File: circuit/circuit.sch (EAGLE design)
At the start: 76 parts

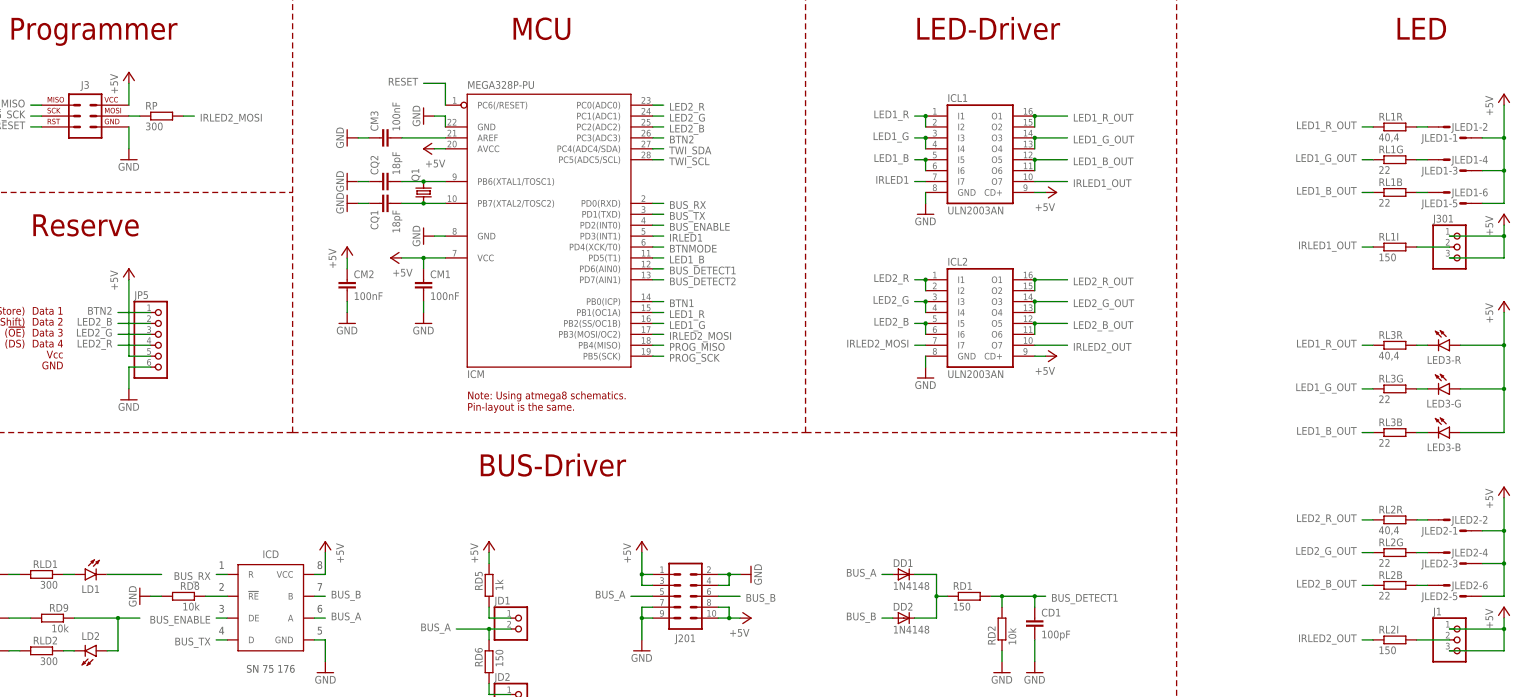
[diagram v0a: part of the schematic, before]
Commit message: updated circuit   + added layout (not done yet)
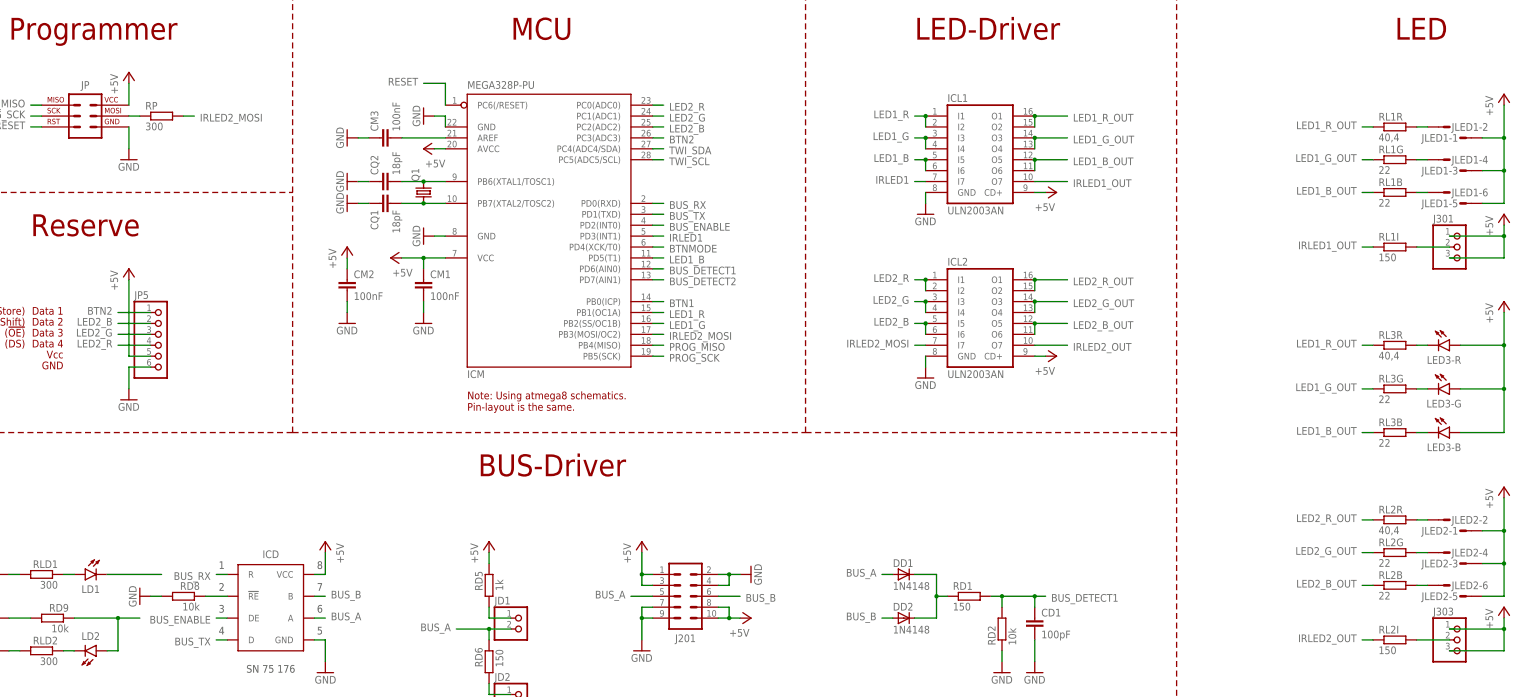
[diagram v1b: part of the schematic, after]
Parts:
- renumbered J1 to J303, J3 to JP
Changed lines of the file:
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@@
 <part name="GND15" library="supply1" deviceset="GND" device=""/>
 <part name="P+6" library="supply1" deviceset="+5V" device=""/>
-<part name="J3" library="robo_ag" deviceset="STECKER_ISP_6" device=""/>
+<part name="JP" library="robo_ag" deviceset="STECKER_ISP_6" device=""/>
 <part name="P+7" library="supply1" deviceset="+5V" device=""/>
 <part name="GND16" library="supply1" deviceset="GND" device=""/>
@@
 <part name="RL2B" library="rcl" deviceset="R-EU_" device="0207/10" value="22"/>
 <part name="P+15" library="supply1" deviceset="+5V" device=""/>
-<part name="J1" library="pinhead" deviceset="PINHD-1X3" device=""/>
+<part name="J303" library="pinhead" deviceset="PINHD-1X3" device=""/>
 <part name="P+17" library="supply1" deviceset="+5V" device=""/>
 <part name="RL3R" library="rcl" deviceset="R-EU_" device="0207/10" value="40,4"/>
@@
 <instance part="GND15" gate="1" x="353.06" y="208.28"/>
 <instance part="P+6" gate="1" x="353.06" y="243.84"/>
-<instance part="J3" gate="ISP" x="33.02" y="172.72"/>
+<instance part="JP" gate="ISP" x="33.02" y="172.72"/>
 <instance part="P+7" gate="1" x="111.76" y="165.1" rot="R90"/>
 <instance part="GND16" gate="1" x="93.98" y="167.64" rot="R270"/>
@@
 <instance part="RL2B" gate="G$1" x="337.82" y="63.5"/>
 <instance part="P+15" gate="1" x="363.22" y="86.36"/>
-<instance part="J1" gate="A" x="353.06" y="50.8"/>
+<instance part="J303" gate="A" x="353.06" y="50.8"/>
 <instance part="P+17" gate="1" x="363.22" y="58.42"/>
 <instance part="RL3R" gate="G$1" x="337.82" y="119.38"/>
@@
 </segment>
 <segment>
-<pinref part="J1" gate="A" pin="3"/>
+<pinref part="J303" gate="A" pin="3"/>
 <wire x1="350.52" y1="48.26" x2="363.22" y2="48.26" width="0.1524" layer="91"/>
 <wire x1="363.22" y1="53.34" x2="363.22" y2="48.26" width="0.1524" layer="91"/>
-<pinref part="J1" gate="A" pin="1"/>
+<pinref part="J303" gate="A" pin="1"/>
 <wire x1="350.52" y1="53.34" x2="363.22" y2="53.34" width="0.1524" layer="91"/>
 <pinref part="P+17" gate="1" pin="+5V"/>
@@
 </segment>
 <segment>
-<pinref part="J3" gate="ISP" pin="2_VCC"/>
+<pinref part="JP" gate="ISP" pin="2_VCC"/>
 <pinref part="P+20" gate="1" pin="+5V"/>
 <wire x1="43.18" y1="175.26" x2="43.18" y2="180.34" width="0.1524" layer="91"/>
@@
 </segment>
 <segment>
-<pinref part="J3" gate="ISP" pin="6_GND"/>
+<pinref part="JP" gate="ISP" pin="6_GND"/>
 <pinref part="GND27" gate="1" pin="GND"/>
 <wire x1="43.18" y1="170.18" x2="43.18" y2="165.1" width="0.1524" layer="91"/>
@@
 </segment>
 <segment>
-<pinref part="J3" gate="ISP" pin="5_RST"/>
+<pinref part="JP" gate="ISP" pin="5_RST"/>
 <wire x1="22.86" y1="170.18" x2="20.32" y2="170.18" width="0.1524" layer="91"/>
 <label x="19.05" y="171.45" size="1.778" layer="91" rot="R180"/>
@@
 </segment>
 <segment>
-<pinref part="J3" gate="ISP" pin="1_MISO"/>
+<pinref part="JP" gate="ISP" pin="1_MISO"/>
 <wire x1="22.86" y1="175.26" x2="20.32" y2="175.26" width="0.1524" layer="91"/>
 <label x="19.05" y="176.53" size="1.778" layer="91" rot="R180"/>
@@
 </segment>
 <segment>
-<pinref part="J3" gate="ISP" pin="3_SCK"/>
+<pinref part="JP" gate="ISP" pin="3_SCK"/>
 <wire x1="22.86" y1="172.72" x2="20.32" y2="172.72" width="0.1524" layer="91"/>
 <label x="19.05" y="173.99" size="1.778" layer="91" rot="R180"/>
@@
 <net name="N$22" class="0">
 <segment>
-<pinref part="J1" gate="A" pin="2"/>
+<pinref part="J303" gate="A" pin="2"/>
 <wire x1="350.52" y1="50.8" x2="342.9" y2="50.8" width="0.1524" layer="91"/>
 <pinref part="RL2I" gate="G$1" pin="2"/>
@@
 <net name="PROG_MOSI_1" class="0">
 <segment>
-<pinref part="J3" gate="ISP" pin="4_MOSI"/>
+<pinref part="JP" gate="ISP" pin="4_MOSI"/>
 <wire x1="43.18" y1="172.72" x2="45.72" y2="172.72" width="0.1524" layer="91"/>
 <pinref part="RP" gate="G$1" pin="1"/>

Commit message: updated circuit   + layout is done   + updated export files
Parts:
- removed JP5: (no value), pinhead:PINHD-1X6/90
- added JP6: (no value), pinhead:PINHD-1X6/90
- added JT: (no value), pinhead:PINHD-1X4
- RD2: value 10k -> 100k
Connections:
- net +5V: now also JP6.5, LD1.A; no longer JP5.5
- net BTN2: now also JP6.1; no longer JP5.1
- net BUS_ENABLE: now also RLD2.1; no longer LD2.A
- net BUS_RX: now also RLD1.2; no longer LD1.C
- net GND: now also JP6.6, LD2.C; no longer JP5.6, RLD1.2, RLD2.2
- net LED2_B: now also JP6.2; no longer JP5.2
- net LED2_G: now also JP6.3; no longer JP5.3
- net LED2_R: now also JP6.4; no longer JP5.4
- net N$34: now also LD1.C, RLD1.1; no longer LD2.C, RLD2.1
- net N$37: now also LD2.A, RLD2.2; no longer LD1.A, RLD1.1
- net TWI_SCL: now also JT.1, JT.4
- net TWI_SDA: now also JT.2, JT.3
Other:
- note added: "Note: SN75176 & ADM485 share the same layout."
- note added: "Note: Value of RD3 and RD4 depend on ICD! SN75176: RD3= ; RD4= ADM485: RD3= ; RD4="
- moved on the sheet: LD1, LD2, RD9, RLD1, RLD2

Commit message: finished layout and exported data
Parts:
- added JD4: (no value), pinhead:PINHD-1X2
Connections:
- net BUS_DETECT1: now also JD4.2
- net LED2_R: now also JD4.1
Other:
- note added: "Note: Possible extended Bus-Detection through ADC-Pin 0. E.g. Idle-Detection. Only if in single-light-mode (not 2 lights). ==> Therefore using a jumper"
- moved on the sheet: CD1, DD1, DD2, RD1, RD2
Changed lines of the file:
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@@
 <part name="P+29" library="supply1" deviceset="+5V" device=""/>
 <part name="JT" library="pinhead" deviceset="PINHD-1X4" device=""/>
+<part name="JD4" library="pinhead" deviceset="PINHD-1X2" device=""/>
 </parts>
 <sheets>
@@
 SN75176: RD3=  ;  RD4=
 ADM485: RD3=  ;  RD4=</text>
+<text x="231.14" y="78.74" size="1.778" layer="94">Note: Possible extended Bus-Detection
+through ADC-Pin 0. E.g. Idle-Detection.
+Only if in single-light-mode (not 2 lights).
+==&gt; Therefore using a jumper</text>
 </plain>
 <instances>
@@
 <instance part="CQ2" gate="G$1" x="101.6" y="157.48" rot="R90"/>
 <instance part="ICL1" gate="A" x="241.3" y="165.1"/>
-<instance part="DD1" gate="G$1" x="223.52" y="66.04" smashed="yes">
-<attribute name="NAME" x="220.98" y="67.7926" size="1.778" layer="95"/>
-<attribute name="VALUE" x="220.98" y="62.4586" size="1.778" layer="96"/>
+<instance part="DD1" gate="G$1" x="223.52" y="60.96" smashed="yes">
+<attribute name="NAME" x="220.98" y="62.7126" size="1.778" layer="95"/>
+<attribute name="VALUE" x="220.98" y="57.3786" size="1.778" layer="96"/>
 </instance>
-<instance part="DD2" gate="G$1" x="223.52" y="55.88" smashed="yes">
-<attribute name="NAME" x="220.98" y="57.6326" size="1.778" layer="95"/>
-<attribute name="VALUE" x="220.98" y="52.2986" size="1.778" layer="96"/>
+<instance part="DD2" gate="G$1" x="223.52" y="50.8" smashed="yes">
+<attribute name="NAME" x="220.98" y="52.5526" size="1.778" layer="95"/>
+<attribute name="VALUE" x="220.98" y="47.2186" size="1.778" layer="96"/>
 </instance>
 <instance part="B1" gate="1" x="170.18" y="218.44"/>
@@
 <instance part="LD1" gate="LED" x="20.32" y="66.04" rot="MR0"/>
 <instance part="RLD1" gate="G$1" x="20.32" y="53.34" rot="MR270"/>
-<instance part="RD1" gate="G$1" x="238.76" y="60.96"/>
-<instance part="CD1" gate="G$1" x="254" y="55.88"/>
-<instance part="GND39" gate="1" x="246.38" y="43.18"/>
-<instance part="RD2" gate="G$1" x="246.38" y="53.34" rot="R90"/>
-<instance part="GND40" gate="1" x="254" y="43.18"/>
+<instance part="RD1" gate="G$1" x="238.76" y="55.88"/>
+<instance part="CD1" gate="G$1" x="254" y="50.8"/>
+<instance part="GND39" gate="1" x="246.38" y="38.1"/>
+<instance part="RD2" gate="G$1" x="246.38" y="48.26" rot="R90"/>
+<instance part="GND40" gate="1" x="254" y="38.1"/>
 <instance part="RD3" gate="G$1" x="238.76" y="27.94"/>
 <instance part="CD2" gate="G$1" x="254" y="22.86"/>
@@
 <instance part="P+29" gate="1" x="20.32" y="73.66" rot="MR0"/>
 <instance part="JT" gate="A" x="53.34" y="121.92" rot="R180"/>
+<instance part="JD4" gate="G$1" x="248.92" y="68.58" rot="R270"/>
 </instances>
 <busses>
@@
 <pinref part="GND39" gate="1" pin="GND"/>
 <pinref part="RD2" gate="G$1" pin="1"/>
-<wire x1="246.38" y1="48.26" x2="246.38" y2="45.72" width="0.1524" layer="91"/>
+<wire x1="246.38" y1="43.18" x2="246.38" y2="40.64" width="0.1524" layer="91"/>
 </segment>
 <segment>
 <pinref part="CD1" gate="G$1" pin="2"/>
 <pinref part="GND40" gate="1" pin="GND"/>
-<wire x1="254" y1="50.8" x2="254" y2="45.72" width="0.1524" layer="91"/>
+<wire x1="254" y1="45.72" x2="254" y2="40.64" width="0.1524" layer="91"/>
 </segment>
 <segment>
@@
 <pinref part="RD1" gate="G$1" pin="2"/>
 <pinref part="CD1" gate="G$1" pin="1"/>
-<wire x1="243.84" y1="60.96" x2="246.38" y2="60.96" width="0.1524" layer="91"/>
+<wire x1="243.84" y1="55.88" x2="246.38" y2="55.88" width="0.1524" layer="91"/>
 <pinref part="RD2" gate="G$1" pin="2"/>
-<wire x1="246.38" y1="58.42" x2="246.38" y2="60.96" width="0.1524" layer="91"/>
-<junction x="246.38" y="60.96"/>
-<wire x1="254" y1="58.42" x2="254" y2="60.96" width="0.1524" layer="91"/>
-<wire x1="254" y1="60.96" x2="246.38" y2="60.96" width="0.1524" layer="91"/>
-<wire x1="254" y1="60.96" x2="256.54" y2="60.96" width="0.1524" layer="91"/>
-<junction x="254" y="60.96"/>
-<label x="257.81" y="59.69" size="1.778" layer="91"/>
+<wire x1="246.38" y1="53.34" x2="246.38" y2="55.88" width="0.1524" layer="91"/>
+<junction x="246.38" y="55.88"/>
+<wire x1="254" y1="53.34" x2="254" y2="55.88" width="0.1524" layer="91"/>
+<wire x1="254" y1="55.88" x2="246.38" y2="55.88" width="0.1524" layer="91"/>
+<wire x1="254" y1="55.88" x2="256.54" y2="55.88" width="0.1524" layer="91"/>
+<junction x="254" y="55.88"/>
+<label x="257.81" y="54.61" size="1.778" layer="91"/>
+</segment>
+<segment>
+<pinref part="JD4" gate="G$1" pin="2"/>
+<wire x1="248.92" y1="71.12" x2="241.3" y2="71.12" width="0.1524" layer="91"/>
+<label x="240.03" y="72.39" size="1.778" layer="91" rot="R180"/>
 </segment>
 </net>
@@
 <pinref part="JP6" gate="A" pin="4"/>
 </segment>
+<segment>
+<pinref part="JD4" gate="G$1" pin="1"/>
+<wire x1="251.46" y1="71.12" x2="259.08" y2="71.12" width="0.1524" layer="91"/>
+<label x="260.35" y="69.85" size="1.778" layer="91"/>
+</segment>
 </net>
 <net name="N$14" class="0">
@@
 </segment>
 <segment>
-<wire x1="220.98" y1="66.04" x2="218.44" y2="66.04" width="0.1524" layer="91"/>
-<label x="217.17" y="67.31" size="1.778" layer="91" rot="R180"/>
+<wire x1="220.98" y1="60.96" x2="218.44" y2="60.96" width="0.1524" layer="91"/>
+<label x="217.17" y="62.23" size="1.778" layer="91" rot="R180"/>
 <pinref part="DD1" gate="G$1" pin="A"/>
 </segment>
@@
 </segment>
 <segment>
-<wire x1="218.44" y1="55.88" x2="220.98" y2="55.88" width="0.1524" layer="91"/>
-<label x="217.17" y="57.15" size="1.778" layer="91" rot="R180"/>
+<wire x1="218.44" y1="50.8" x2="220.98" y2="50.8" width="0.1524" layer="91"/>
+<label x="217.17" y="52.07" size="1.778" layer="91" rot="R180"/>
 <pinref part="DD2" gate="G$1" pin="A"/>
 </segment>
@@
 <segment>
 <pinref part="DD1" gate="G$1" pin="C"/>
-<wire x1="226.06" y1="66.04" x2="231.14" y2="66.04" width="0.1524" layer="91"/>
-<wire x1="231.14" y1="66.04" x2="231.14" y2="60.96" width="0.1524" layer="91"/>
+<wire x1="226.06" y1="60.96" x2="231.14" y2="60.96" width="0.1524" layer="91"/>
+<wire x1="231.14" y1="60.96" x2="231.14" y2="55.88" width="0.1524" layer="91"/>
 <pinref part="DD2" gate="G$1" pin="C"/>
-<wire x1="231.14" y1="60.96" x2="231.14" y2="55.88" width="0.1524" layer="91"/>
-<wire x1="231.14" y1="55.88" x2="226.06" y2="55.88" width="0.1524" layer="91"/>
-<wire x1="231.14" y1="60.96" x2="233.68" y2="60.96" width="0.1524" layer="91"/>
-<junction x="231.14" y="60.96"/>
+<wire x1="231.14" y1="55.88" x2="231.14" y2="50.8" width="0.1524" layer="91"/>
+<wire x1="231.14" y1="50.8" x2="226.06" y2="50.8" width="0.1524" layer="91"/>
+<wire x1="231.14" y1="55.88" x2="233.68" y2="55.88" width="0.1524" layer="91"/>
+<junction x="231.14" y="55.88"/>
 <pinref part="RD1" gate="G$1" pin="1"/>
 </segment>
